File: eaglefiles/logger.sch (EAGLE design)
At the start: 39 parts, among them K1 65100516121, Q2 IRLML9301, U1 MCP1640, U3 FT232RLSSOP

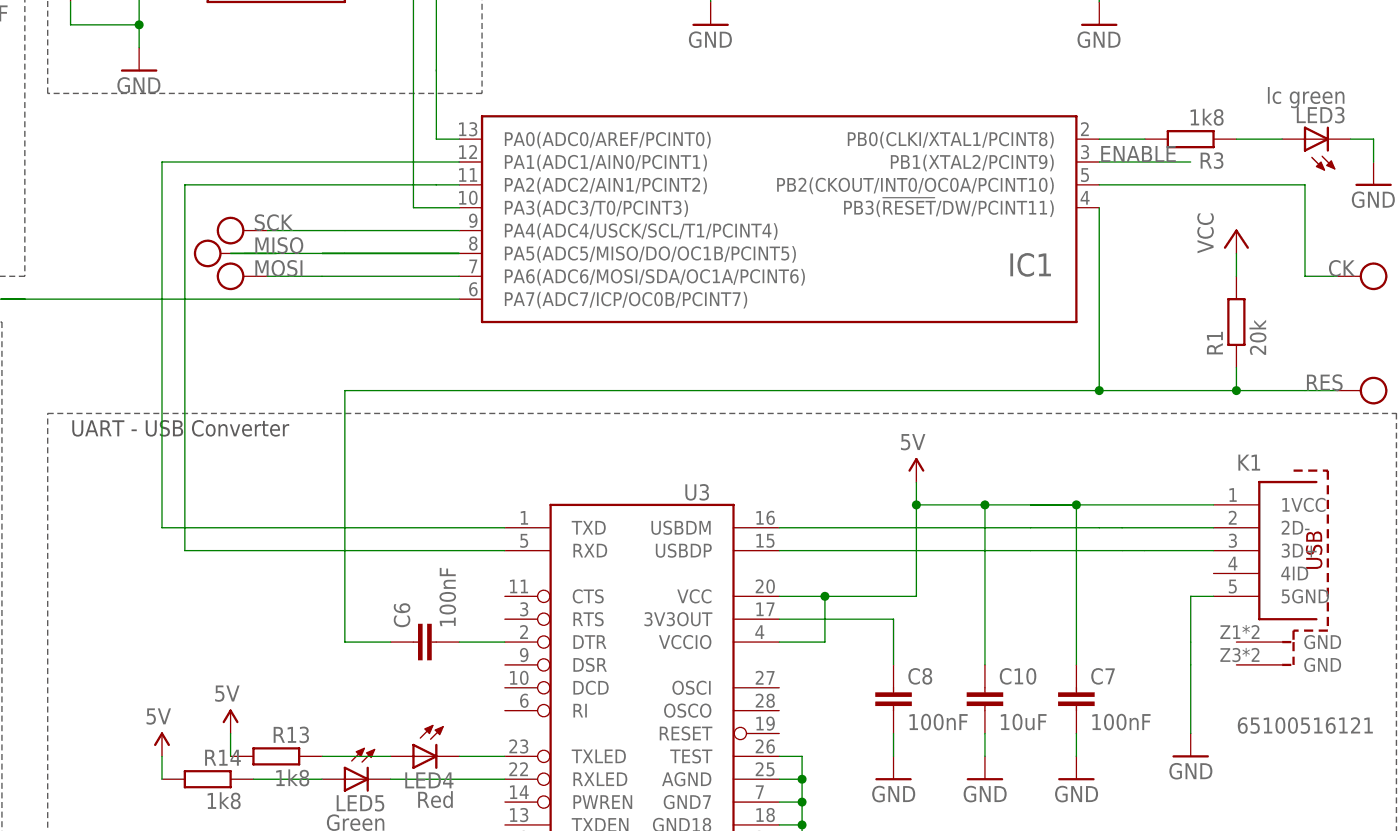
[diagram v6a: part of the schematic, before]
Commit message: Fixed failure in schematic: TX and RX mixed up...
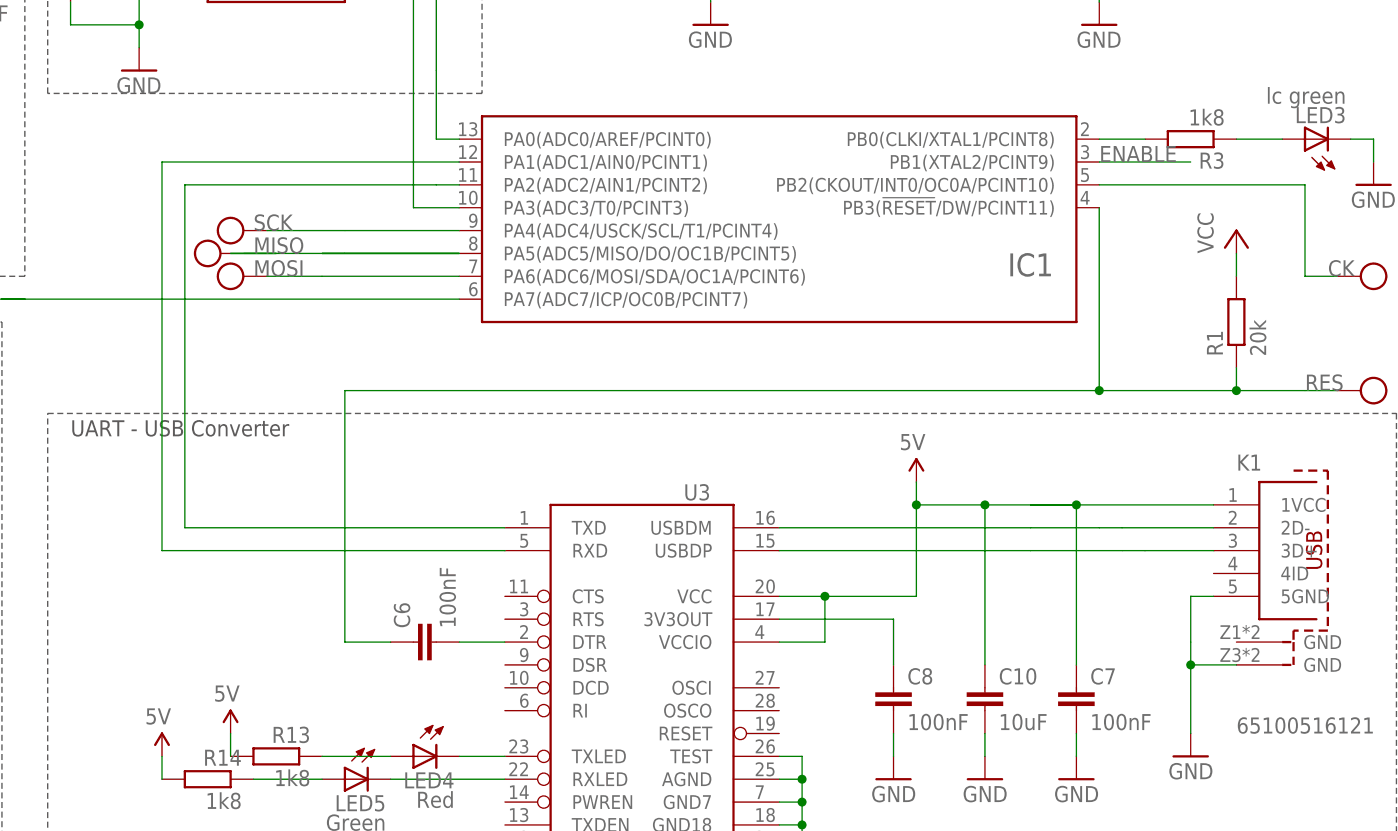
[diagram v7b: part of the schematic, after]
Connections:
- net GND: now also K1.GND@2
- net N$1: now also U3.TXD; no longer U3.RXD
- net N$32: now also U3.RXD; no longer U3.TXD
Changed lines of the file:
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@@
 <wire x1="129.54" y1="-30.48" x2="129.54" y2="-33.02" width="0.1524" layer="91"/>
 <wire x1="129.54" y1="-33.02" x2="129.54" y2="-40.64" width="0.1524" layer="91"/>
+<pinref part="K1" gate="G$1" pin="GND@2"/>
+<wire x1="134.62" y1="-33.02" x2="129.54" y2="-33.02" width="0.1524" layer="91"/>
+<junction x="129.54" y="-33.02"/>
 </segment>
 <segment>
@@
 <pinref part="IC1" gate="IC" pin="PA1(ADC1/AIN0/PCINT1)"/>
 <wire x1="15.24" y1="22.86" x2="48.26" y2="22.86" width="0.1524" layer="91"/>
-<wire x1="15.24" y1="22.86" x2="15.24" y2="-17.78" width="0.1524" layer="91"/>
-<pinref part="U3" gate="G$1" pin="TXD"/>
-<wire x1="15.24" y1="-17.78" x2="53.34" y2="-17.78" width="0.1524" layer="91"/>
+<wire x1="15.24" y1="22.86" x2="15.24" y2="-20.32" width="0.1524" layer="91"/>
+<pinref part="U3" gate="G$1" pin="RXD"/>
+<wire x1="15.24" y1="-20.32" x2="53.34" y2="-20.32" width="0.1524" layer="91"/>
 </segment>
 </net>
@@
 <wire x1="48.26" y1="20.32" x2="45.72" y2="20.32" width="0.1524" layer="91"/>
 <wire x1="45.72" y1="20.32" x2="17.78" y2="20.32" width="0.1524" layer="91"/>
-<wire x1="17.78" y1="20.32" x2="17.78" y2="-20.32" width="0.1524" layer="91"/>
-<pinref part="U3" gate="G$1" pin="RXD"/>
-<wire x1="17.78" y1="-20.32" x2="53.34" y2="-20.32" width="0.1524" layer="91"/>
+<wire x1="17.78" y1="20.32" x2="17.78" y2="-17.78" width="0.1524" layer="91"/>
+<pinref part="U3" gate="G$1" pin="TXD"/>
+<wire x1="17.78" y1="-17.78" x2="53.34" y2="-17.78" width="0.1524" layer="91"/>
 </segment>
 </net>

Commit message: Fixed wrong signal
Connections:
- removed net 5V: D3.A, R2.1, R4.1
- new net BATOFF: C9.1, Q2.G, R4.2
- net V_USB: now also D3.A, R2.1, R4.1; no longer C9.1, Q2.G, R4.2
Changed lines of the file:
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@@
 </segment>
 <segment>
-<wire x1="-25.4" y1="-10.16" x2="-33.02" y2="-10.16" width="0.1524" layer="91"/>
-<wire x1="-33.02" y1="-10.16" x2="-35.56" y2="-10.16" width="0.1524" layer="91"/>
-<pinref part="Q2" gate="G$1" pin="G"/>
-<pinref part="C9" gate="G$1" pin="1"/>
-<wire x1="-30.48" y1="-20.32" x2="-33.02" y2="-20.32" width="0.1524" layer="91"/>
-<wire x1="-33.02" y1="-20.32" x2="-33.02" y2="-10.16" width="0.1524" layer="91"/>
-<junction x="-33.02" y="-10.16"/>
-<pinref part="R4" gate="G$1" pin="2"/>
+<pinref part="R2" gate="G$1" pin="1"/>
+<pinref part="R4" gate="G$1" pin="1"/>
+<wire x1="-45.72" y1="-10.16" x2="-48.26" y2="-10.16" width="0.1524" layer="91"/>
+<wire x1="-48.26" y1="-10.16" x2="-53.34" y2="-10.16" width="0.1524" layer="91"/>
+<wire x1="-53.34" y1="-10.16" x2="-53.34" y2="-15.24" width="0.1524" layer="91"/>
+<junction x="-53.34" y="-10.16"/>
+<wire x1="-53.34" y1="-10.16" x2="-53.34" y2="-7.62" width="0.1524" layer="91"/>
+<pinref part="U$6" gate="G$1" pin="5V"/>
+<pinref part="D3" gate="1" pin="A"/>
+<wire x1="-48.26" y1="-10.16" x2="-48.26" y2="-7.62" width="0.1524" layer="91"/>
+<junction x="-48.26" y="-10.16"/>
 </segment>
 </net>
@@
 <wire x1="-20.32" y1="-12.7" x2="-20.32" y2="-20.32" width="0.1524" layer="91"/>
 <junction x="-20.32" y="-20.32"/>
-</segment>
-</net>
-<net name="5V" class="0">
-<segment>
-<pinref part="R2" gate="G$1" pin="1"/>
-<pinref part="R4" gate="G$1" pin="1"/>
-<wire x1="-45.72" y1="-10.16" x2="-48.26" y2="-10.16" width="0.1524" layer="91"/>
-<wire x1="-48.26" y1="-10.16" x2="-53.34" y2="-10.16" width="0.1524" layer="91"/>
-<wire x1="-53.34" y1="-10.16" x2="-53.34" y2="-15.24" width="0.1524" layer="91"/>
-<junction x="-53.34" y="-10.16"/>
-<wire x1="-53.34" y1="-10.16" x2="-53.34" y2="-7.62" width="0.1524" layer="91"/>
-<pinref part="U$6" gate="G$1" pin="5V"/>
-<pinref part="D3" gate="1" pin="A"/>
-<wire x1="-48.26" y1="-10.16" x2="-48.26" y2="-7.62" width="0.1524" layer="91"/>
-<junction x="-48.26" y="-10.16"/>
 </segment>
 </net>
@@
 </segment>
 </net>
+<net name="BATOFF" class="0">
+<segment>
+<wire x1="-25.4" y1="-10.16" x2="-33.02" y2="-10.16" width="0.1524" layer="91"/>
+<pinref part="Q2" gate="G$1" pin="G"/>
+<pinref part="C9" gate="G$1" pin="1"/>
+<wire x1="-30.48" y1="-20.32" x2="-33.02" y2="-20.32" width="0.1524" layer="91"/>
+<wire x1="-33.02" y1="-20.32" x2="-33.02" y2="-10.16" width="0.1524" layer="91"/>
+<pinref part="R4" gate="G$1" pin="2"/>
+<wire x1="-33.02" y1="-10.16" x2="-35.56" y2="-10.16" width="0.1524" layer="91"/>
+<junction x="-33.02" y="-10.16"/>
+</segment>
+</net>
